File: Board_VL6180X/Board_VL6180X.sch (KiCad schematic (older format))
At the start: 11 parts, among them J1 Conn_01x06

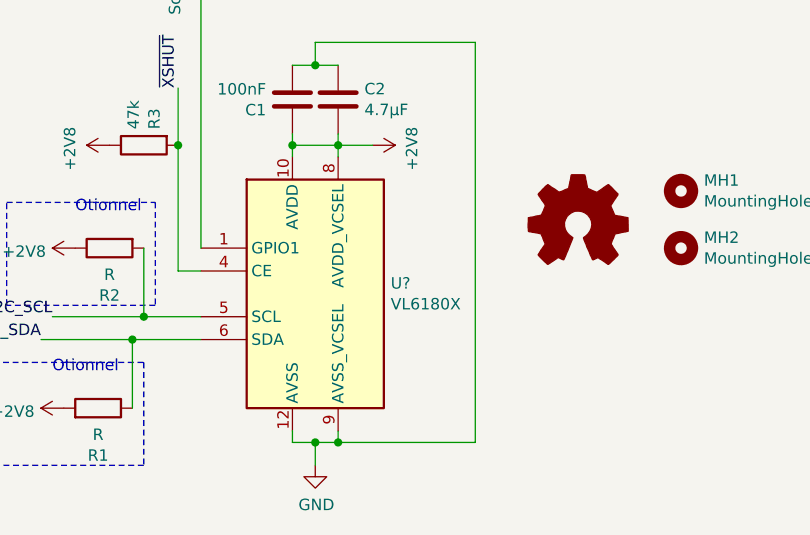
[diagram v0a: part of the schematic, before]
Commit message: PCB VL6180X done
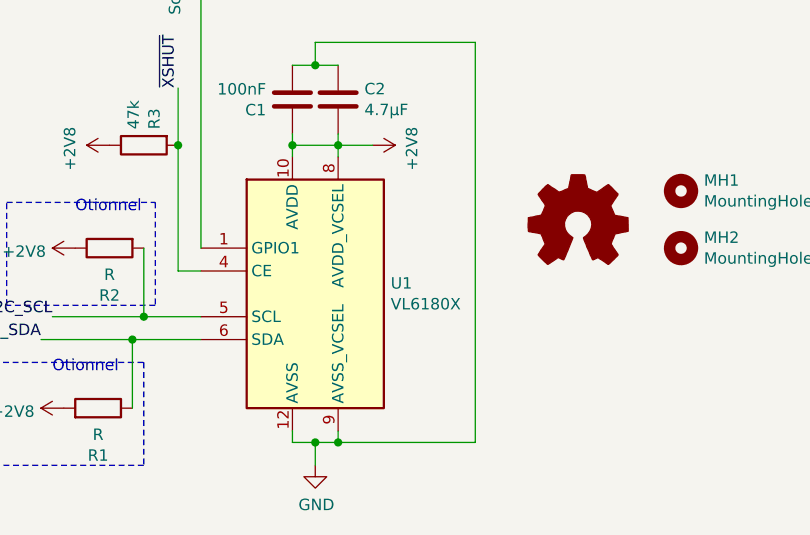
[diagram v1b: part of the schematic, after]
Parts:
- U1: renamed from U?; footprint PhoenixRobotik:TOF-12_4.4x2.4x1.0mm_P0.8mm -> PhoenixRobotik:ST_LGA-12_2.8x4.8x1.0mm_P0.75mm
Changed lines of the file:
@@
 EESchema Schematic File Version 4
+LIBS:Board_VL6180X-cache
 EELAYER 26 0
 EELAYER END
@@
 	4200 4000 4500 4000
 $Comp
-L PhoenixRobotik:VL6180X U?
+L PhoenixRobotik:VL6180X U1
 U 1 1 5BD5E1D7
 P 5000 3800
-F 0 "U?" H 5330 3846 50  0000 L CNN
+F 0 "U1" H 5330 3846 50  0000 L CNN
 F 1 "VL6180X" H 5330 3755 50  0000 L CNN
-F 2 "PhoenixRobotik:TOF-12_4.4x2.4x1.0mm_P0.8mm" H 6200 3300 50  0001 C CNN
+F 2 "PhoenixRobotik:ST_LGA-12_2.8x4.8x1.0mm_P0.75mm" H 6200 3300 50  0001 C CNN
 F 3 "https://www.st.com/resource/en/datasheet/vl6180x.pdf" H 6200 3200 50  0001 C CNN
 	1    5000 3800

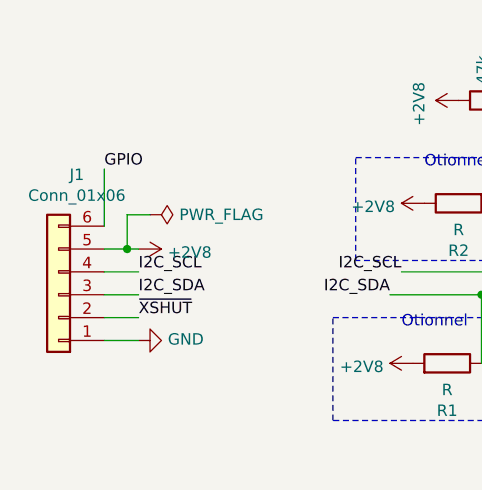
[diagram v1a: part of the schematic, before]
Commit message: Changed JST connectors
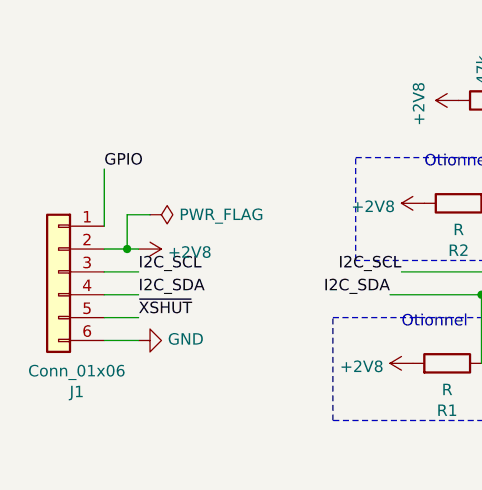
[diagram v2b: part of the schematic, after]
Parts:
- J1: footprint Connector_JST:JST_PH_B6B-PH-K_1x06_P2.00mm_Vertical -> Connector_JST:JST_PH_S6B-PH-K_1x06_P2.00mm_Horizontal
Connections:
- net +2V8: now also J1.2 (Pin_2); no longer J1.5 (Pin_5)
- net GND: now also J1.6 (Pin_6); no longer J1.1 (Pin_1)
- net GPIO: now also J1.1 (Pin_1); no longer J1.6 (Pin_6)
- net I2C_SCL: now also J1.3 (Pin_3); no longer J1.4 (Pin_4)
- net I2C_SDA: now also J1.4 (Pin_4); no longer J1.3 (Pin_3)
- net ~XSHUT: now also J1.5 (Pin_5); no longer J1.2 (Pin_2)
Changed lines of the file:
@@
 L Connector_Generic:Conn_01x06 J1
 U 1 1 5BC3B9FD
-P 2350 4000
-F 0 "J1" H 2270 3475 50  0000 C CNN
-F 1 "Conn_01x06" H 2270 3566 50  0000 C CNN
-F 2 "Connector_JST:JST_PH_B6B-PH-K_1x06_P2.00mm_Vertical" H 2350 4000 50  0001 C CNN
-F 3 "~" H 2350 4000 50  0001 C CNN
-	1    2350 4000
-	-1   0    0    1
+P 2350 3900
+F 0 "J1" H 2270 3375 50  0000 C CNN
+F 1 "Conn_01x06" H 2270 3466 50  0000 C CNN
+F 2 "Connector_JST:JST_PH_S6B-PH-K_1x06_P2.00mm_Horizontal" H 2350 3900 50  0001 C CNN
+F 3 "~" H 2350 3900 50  0001 C CNN
+	1    2350 3900
+	-1   0    0    -1
 $EndComp
 Text Label 2550 3450 0    50   ~ 0

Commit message: update board
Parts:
- removed MH1, MH2: MountingHole, MountingHole:MountingHole_2.2mm_M2, symbol Mechanical:MountingHole
- added MH1, MH2: MountingHole_Pad, MountingHole:MountingHole_2.2mm_M2_Pad, symbol Mechanical:MountingHole_Pad
- U1: footprint PhoenixRobotik:ST_LGA-12_2.8x4.8x1.0mm_P0.75mm -> PhenixRobotik:ST_LGA-12_2.8x4.8x1.0mm_P0.75mm; symbol PhoenixRobotik:VL6180X -> PhenixRobotik:VL6180X
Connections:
- wire segments 38 -> 40
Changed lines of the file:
@@
 EESchema Schematic File Version 4
-LIBS:Board_VL6180X-cache
 EELAYER 26 0
 EELAYER END
@@
 	3650 3850 3650 3400
 $Comp
-L Mechanical:MountingHole MH1
-U 1 1 5BC3ACFC
-P 6600 3350
-F 0 "MH1" H 6700 3396 50  0000 L CNN
-F 1 "MountingHole" H 6700 3305 50  0000 L CNN
-F 2 "MountingHole:MountingHole_2.2mm_M2" H 6600 3350 50  0001 C CNN
-F 3 "~" H 6600 3350 50  0001 C CNN
-	1    6600 3350
-	1    0    0    -1
-$EndComp
-$Comp
-L Mechanical:MountingHole MH2
-U 1 1 5BC3AFD2
-P 6600 3600
-F 0 "MH2" H 6700 3646 50  0000 L CNN
-F 1 "MountingHole" H 6700 3555 50  0000 L CNN
-F 2 "MountingHole:MountingHole_2.2mm_M2" H 6600 3600 50  0001 C CNN
-F 3 "~" H 6600 3600 50  0001 C CNN
-	1    6600 3600
-	1    0    0    -1
-$EndComp
-$Comp
 L Graphic:Logo_Open_Hardware_Small #LOGO1
 U 1 1 5BC3B0F0
@@
 	4200 4000 4500 4000
 $Comp
-L PhoenixRobotik:VL6180X U1
+L PhenixRobotik:VL6180X U1
 U 1 1 5BD5E1D7
 P 5000 3800
 F 0 "U1" H 5330 3846 50  0000 L CNN
 F 1 "VL6180X" H 5330 3755 50  0000 L CNN
-F 2 "PhoenixRobotik:ST_LGA-12_2.8x4.8x1.0mm_P0.75mm" H 6200 3300 50  0001 C CNN
+F 2 "PhenixRobotik:ST_LGA-12_2.8x4.8x1.0mm_P0.75mm" H 6200 3300 50  0001 C CNN
 F 3 "https://www.st.com/resource/en/datasheet/vl6180x.pdf" H 6200 3200 50  0001 C CNN
 	1    5000 3800
@@
 Wire Wire Line
 	5100 4450 5700 4450
+$Comp
+L Mechanical:MountingHole_Pad MH1
+U 1 1 5BE08214
+P 7200 3300
+F 0 "MH1" V 7154 3450 50  0000 L CNN
+F 1 "MountingHole_Pad" V 7245 3450 50  0000 L CNN
+F 2 "MountingHole:MountingHole_2.2mm_M2_Pad" H 7200 3300 50  0001 C CNN
+F 3 "~" H 7200 3300 50  0001 C CNN
+	1    7200 3300
+	0    1    1    0
+$EndComp
+$Comp
+L Mechanical:MountingHole_Pad MH2
+U 1 1 5BE08279
+P 7200 3500
+F 0 "MH2" V 7154 3650 50  0000 L CNN
+F 1 "MountingHole_Pad" V 7245 3650 50  0000 L CNN
+F 2 "MountingHole:MountingHole_2.2mm_M2_Pad" H 7200 3500 50  0001 C CNN
+F 3 "~" H 7200 3500 50  0001 C CNN
+	1    7200 3500
+	0    1    1    0
+$EndComp
+Wire Wire Line
+	7100 3300 7100 3500
+Connection ~ 7100 3500
+Wire Wire Line
+	7100 3500 7100 3700
+$Comp
+L power:GND #PWR?
+U 1 1 5BE08F16
+P 7100 3700
+F 0 "#PWR?" H 7100 3450 50  0001 C CNN
+F 1 "GND" H 7105 3527 50  0000 C CNN
+F 2 "" H 7100 3700 50  0001 C CNN
+F 3 "" H 7100 3700 50  0001 C CNN
+	1    7100 3700
+	1    0    0    -1
+$EndComp
 $EndSCHEMATC

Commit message: add logos
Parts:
- added LOGO1: Logo_Open_Hardware_Small, Symbol:OSHW-Logo2_7.3x6mm_SilkScreen, symbol Graphic:Logo_Open_Hardware_Small
- added LOGO2: Logo_Open_Hardware_Small, PhenixRobotik:Logo_8,5mm, symbol Graphic:Logo_Open_Hardware_Small
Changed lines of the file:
@@
 	3650 3850 3650 3400
 $Comp
-L Graphic:Logo_Open_Hardware_Small #LOGO1
+L Graphic:Logo_Open_Hardware_Small LOGO1
 U 1 1 5BC3B0F0
 P 6150 3500
-F 0 "#LOGO1" H 6150 3775 50  0001 C CNN
+F 0 "LOGO1" H 6150 3775 50  0001 C CNN
 F 1 "Logo_Open_Hardware_Small" H 6150 3275 50  0001 C CNN
-F 2 "" H 6150 3500 50  0001 C CNN
+F 2 "Symbol:OSHW-Logo2_7.3x6mm_SilkScreen" H 6150 3500 50  0001 C CNN
 F 3 "~" H 6150 3500 50  0001 C CNN
 	1    6150 3500
@@
 	7100 3500 7100 3700
 $Comp
-L power:GND #PWR?
+L power:GND #PWR0101
 U 1 1 5BE08F16
 P 7100 3700
-F 0 "#PWR?" H 7100 3450 50  0001 C CNN
+F 0 "#PWR0101" H 7100 3450 50  0001 C CNN
 F 1 "GND" H 7105 3527 50  0000 C CNN
 F 2 "" H 7100 3700 50  0001 C CNN
@@
 	1    0    0    -1
 $EndComp
+$Comp
+L Graphic:Logo_Open_Hardware_Small LOGO2
+U 1 1 5BE09EB9
+P 6600 3500
+F 0 "LOGO2" H 6600 3775 50  0001 C CNN
+F 1 "Logo_Open_Hardware_Small" H 6600 3275 50  0001 C CNN
+F 2 "PhenixRobotik:Logo_8,5mm" H 6600 3500 50  0001 C CNN
+F 3 "~" H 6600 3500 50  0001 C CNN
+	1    6600 3500
+	1    0    0    -1
+$EndComp
